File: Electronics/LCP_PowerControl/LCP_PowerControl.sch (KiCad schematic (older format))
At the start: 0 parts

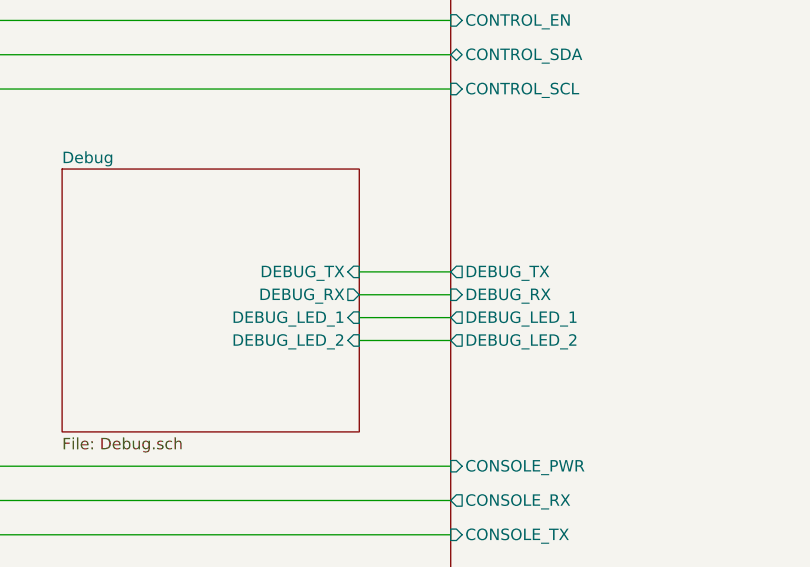
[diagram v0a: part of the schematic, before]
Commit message: Rev1.1 Gerber Upload
Included 3way open solder jumps to choose control of Encoder channels of hall effect sensor
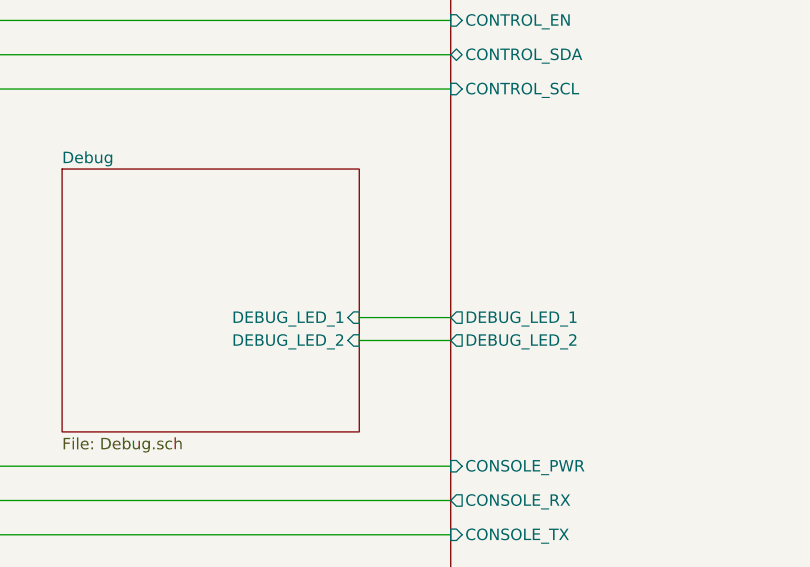
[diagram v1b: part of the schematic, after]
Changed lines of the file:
@@
 F15 "~MD_SLEEP" O R 7000 3400 50
 F16 "12V_ENABLE" O L 4300 2650 50
-F17 "DEBUG_TX" O L 4300 4950 50
-F18 "DEBUG_RX" I L 4300 5050 50
-F19 "DEBUG_LED_1" O L 4300 5150 50
-F20 "DEBUG_LED_2" O L 4300 5250 50
-F21 "ENCODER_CH_A" I R 7000 4550 50
-F22 "ENCODER_CH_B" I R 7000 4650 50
-F23 "CONSOLE_PWR" I L 4300 5800 50
+F17 "DEBUG_LED_1" O L 4300 5150 50
+F18 "DEBUG_LED_2" O L 4300 5250 50
+F19 "ENCODER_CH_A" I R 7000 4550 50
+F20 "ENCODER_CH_B" I R 7000 4650 50
+F21 "CONSOLE_PWR" I L 4300 5800 50
 $EndSheet
 $Sheet
@@
 F0 "Debug" 50
 F1 "Debug.sch" 50
-F2 "DEBUG_TX" I R 3900 4950 50
-F3 "DEBUG_RX" O R 3900 5050 50
-F4 "DEBUG_LED_1" I R 3900 5150 50
-F5 "DEBUG_LED_2" I R 3900 5250 50
+F2 "DEBUG_LED_1" I R 3900 5150 50
+F3 "DEBUG_LED_2" I R 3900 5250 50
 $EndSheet
 Wire Wire Line
@@
 	4300 5150 3900 5150
 Wire Wire Line
-	3900 5050 4300 5050
-Wire Wire Line
-	4300 4950 3900 4950
-Wire Wire Line
 	4300 5800 2200 5800
